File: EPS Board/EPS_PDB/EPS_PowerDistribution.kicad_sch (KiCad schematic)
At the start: 26 parts

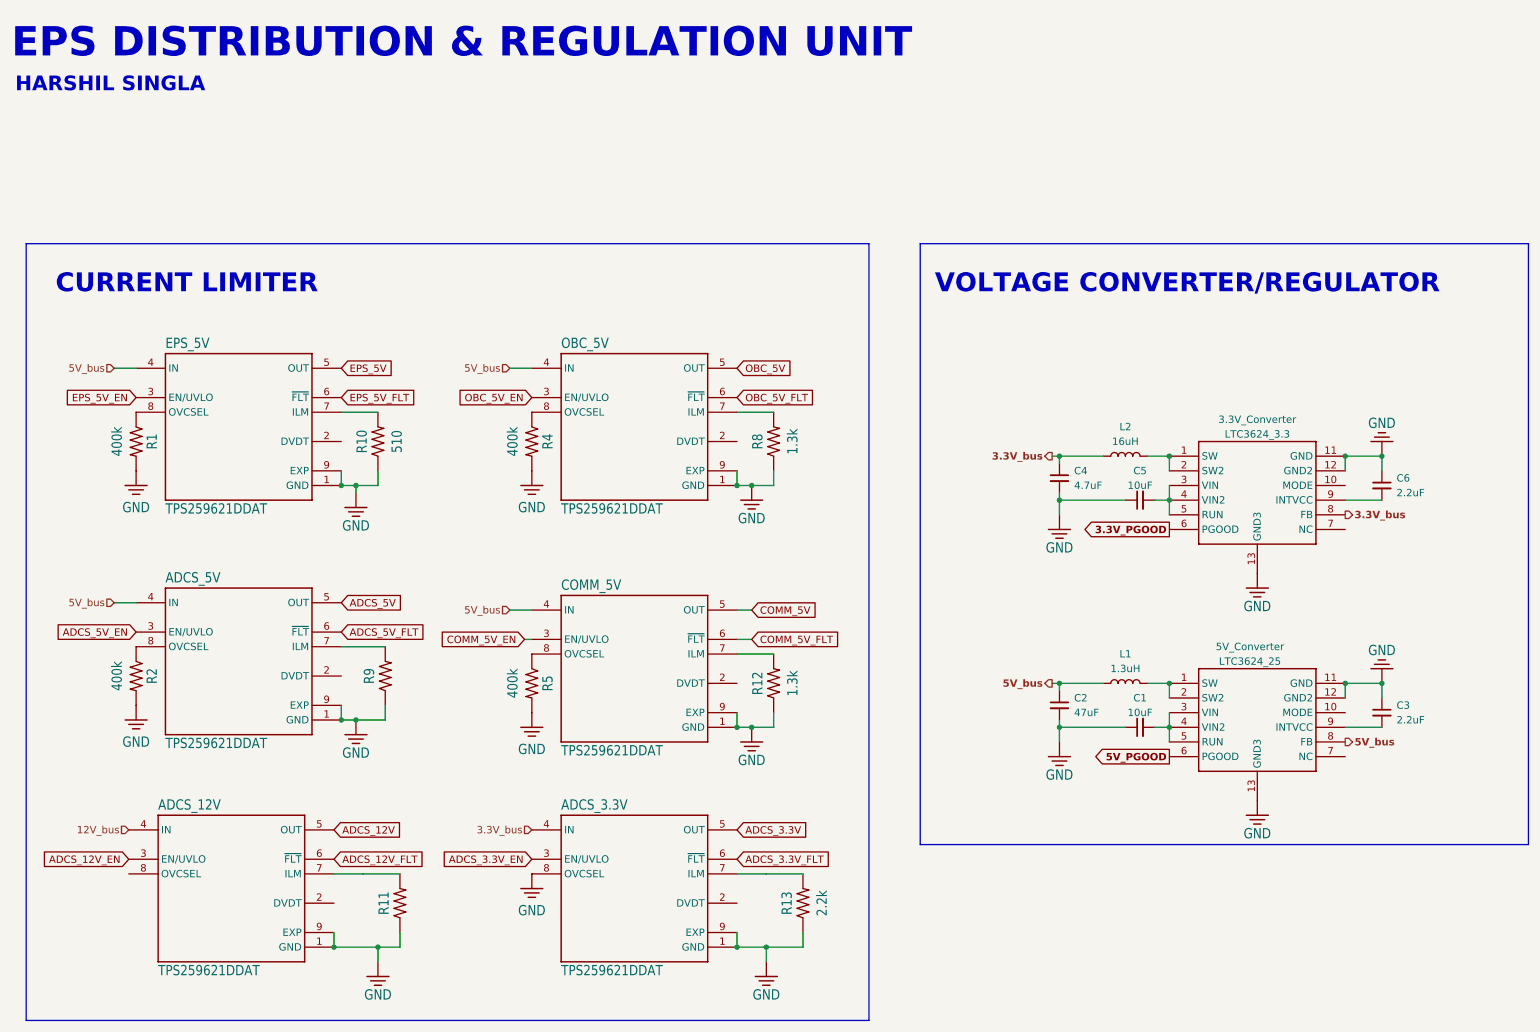
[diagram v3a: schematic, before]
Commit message: Fixed libraries and updated schematic accordingly
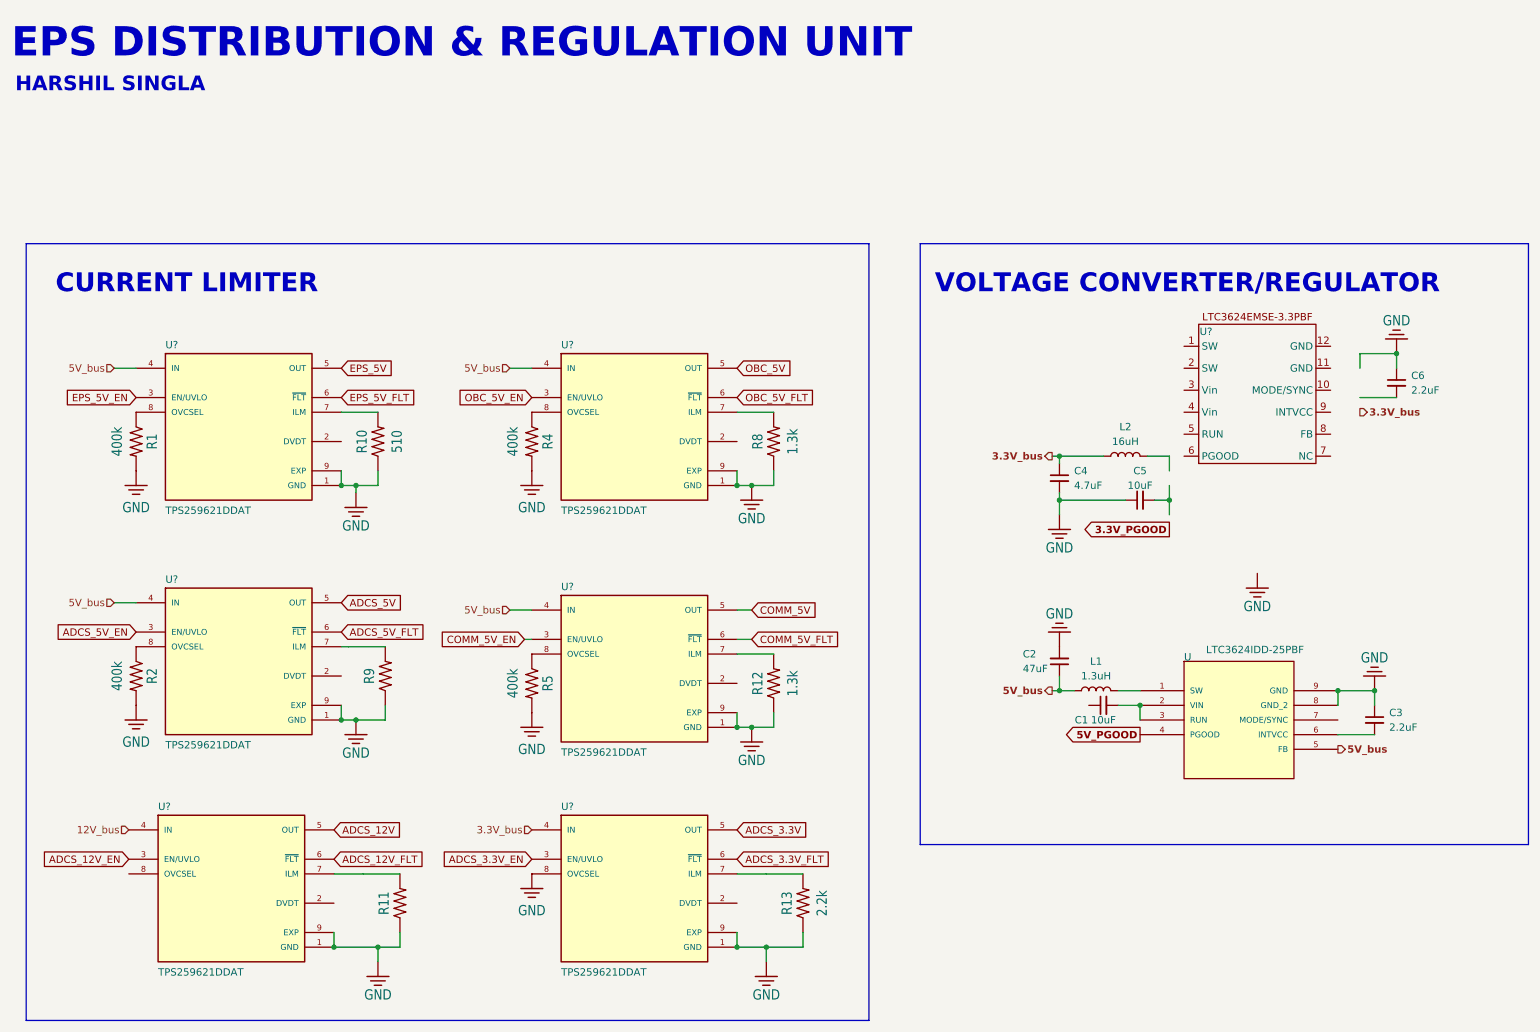
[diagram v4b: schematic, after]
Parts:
- U: renamed from 5V_Converter; value LTC3624_25 -> LTC3624IDD-25PBF; footprint EPS_Schematic_v2:SOP65P490X110-13N -> (none); symbol EPS_Schematic_v2-eagle-import:LTC3624_25 -> LTC3624IDD-25PBF:LTC3624IDD-25PBF
- U?: renamed from OBC_5V; symbol EPS_Schematic_v2-eagle-import:TPS259621DDAT -> TPS259621DDAT:TPS259621DDAT
- U?: renamed from ADCS_5V; symbol EPS_Schematic_v2-eagle-import:TPS259621DDAT -> TPS259621DDAT:TPS259621DDAT
- U?: renamed from ADCS_12V; symbol EPS_Schematic_v2-eagle-import:TPS259621DDAT -> TPS259621DDAT:TPS259621DDAT
- U?: renamed from ADCS_3.3V; symbol EPS_Schematic_v2-eagle-import:TPS259621DDAT -> TPS259621DDAT:TPS259621DDAT
- U?: renamed from EPS_5V; symbol EPS_Schematic_v2-eagle-import:TPS259621DDAT -> TPS259621DDAT:TPS259621DDAT
- U?: renamed from 3.3V_Converter; value LTC3624_3.3 -> (none); symbol EPS_Schematic_v2-eagle-import:LTC3624_3.3 -> LTC3624_3.3:LTC3624EMSE_3.3PBF
- U?: renamed from COMM_5V; symbol EPS_Schematic_v2-eagle-import:TPS259621DDAT -> TPS259621DDAT:TPS259621DDAT
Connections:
- net 3.3V_PGOOD: no longer U?.6 (PGOOD)
- net 3.3V_bus: no longer U?.8 (FB)
- net 5V_PGOOD: now also U.4 (PGOOD); no longer U.6 (PGOOD)
- net 5V_bus: now also U.5 (FB); no longer U.8 (FB)
- net GND: now also U.8 (GND_2), U.9 (GND); no longer C1.1, U.11 (GND), U.12 (GND2), U.13 (GND3), U?.11 (GND), U?.12 (GND2), U?.13 (GND3)
- net at L1.2, U.1 (SW): no longer U.2 (SW2)
- net at C1.2, U.3 (RUN): now also U.2 (VIN); no longer U.4 (VIN2), U.5 (RUN)
- net at C3.2: now also U.6 (INTVCC); no longer U.9 (INTVCC)
- net at C6.2: no longer U?.9 (INTVCC)
- now unconnected: C5.2, L2.2, U?.1 (SW), U?.2 (SW2), U?.3 (VIN), U?.4 (VIN2), U?.5 (RUN)
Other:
- moved on the sheet: C1, C2, C3, C6, L1

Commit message: Added PCB dxf outline
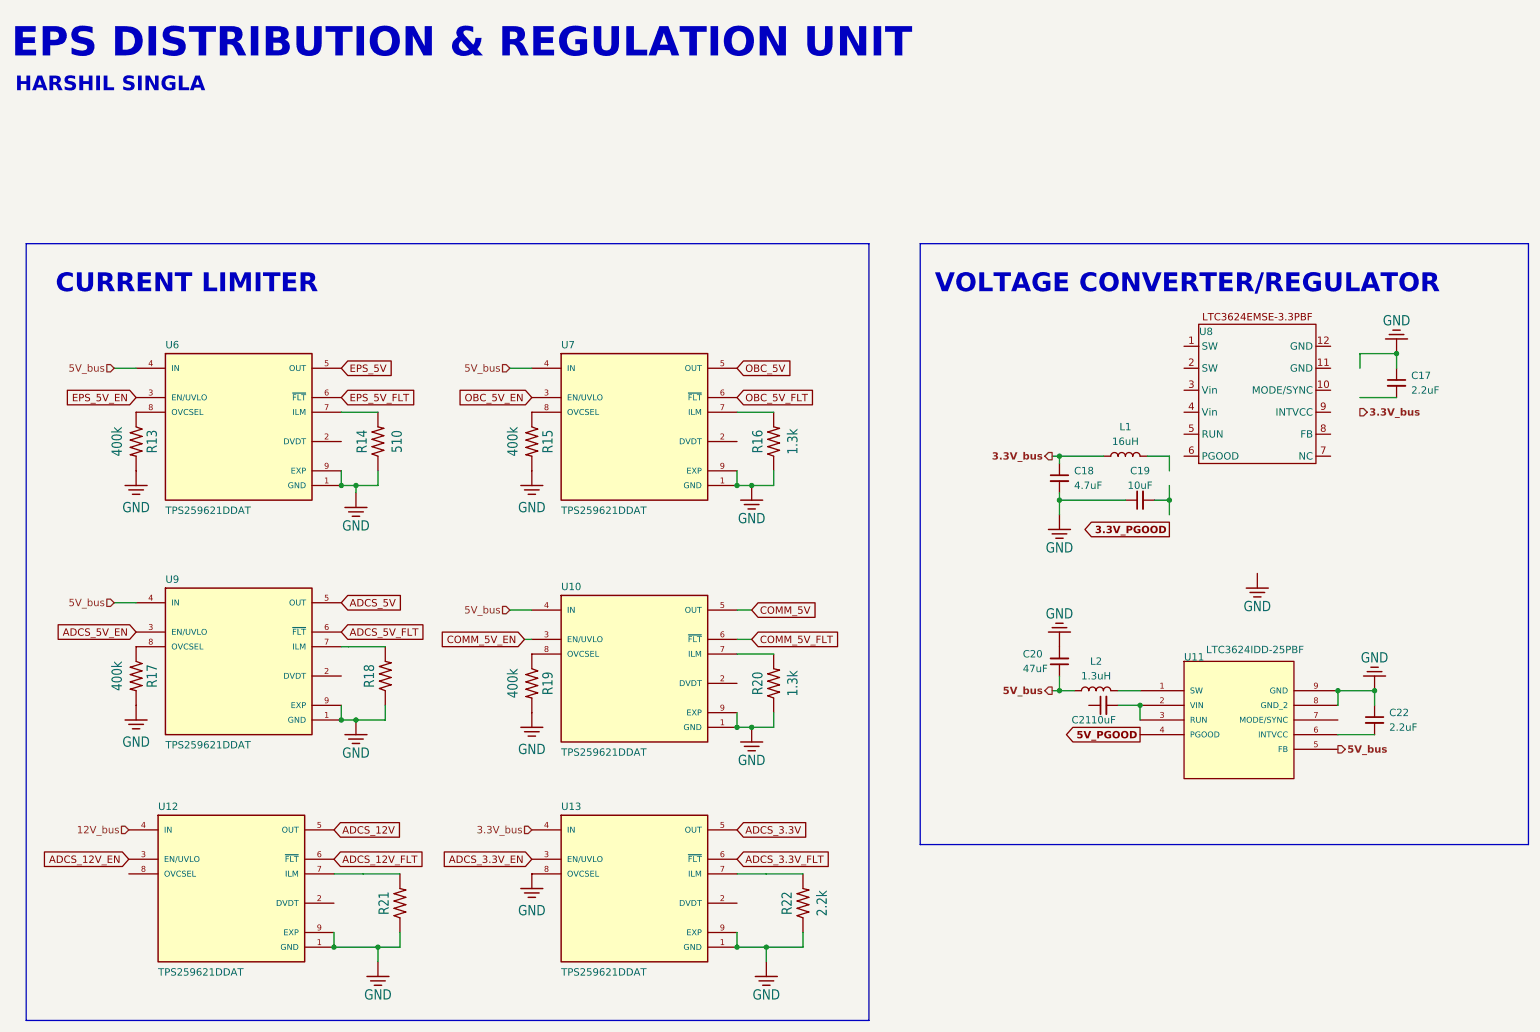
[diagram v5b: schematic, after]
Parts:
- U8: renamed from U?; value (none) -> ~
- gave numbers to parts that had none: 6
- renumbered C6 to C17, C4 to C18, C5 to C19, C2 to C20, C1 to C21, C3 to C22, L2 to L1, L1 to L2, R1 to R13, R10 to R14, R4 to R15, R8 to R16, R2 to R17, R9 to R18, R5 to R19, R12 to R20, R11 to R21, R13 to R22, U to U11
